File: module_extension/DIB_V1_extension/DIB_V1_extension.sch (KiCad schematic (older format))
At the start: 12 parts, among them J1 20-pin power socket, J3 28-pin module socket, J3 PROBE, J4 CABLE, J5 PROBE, J6 CABLE

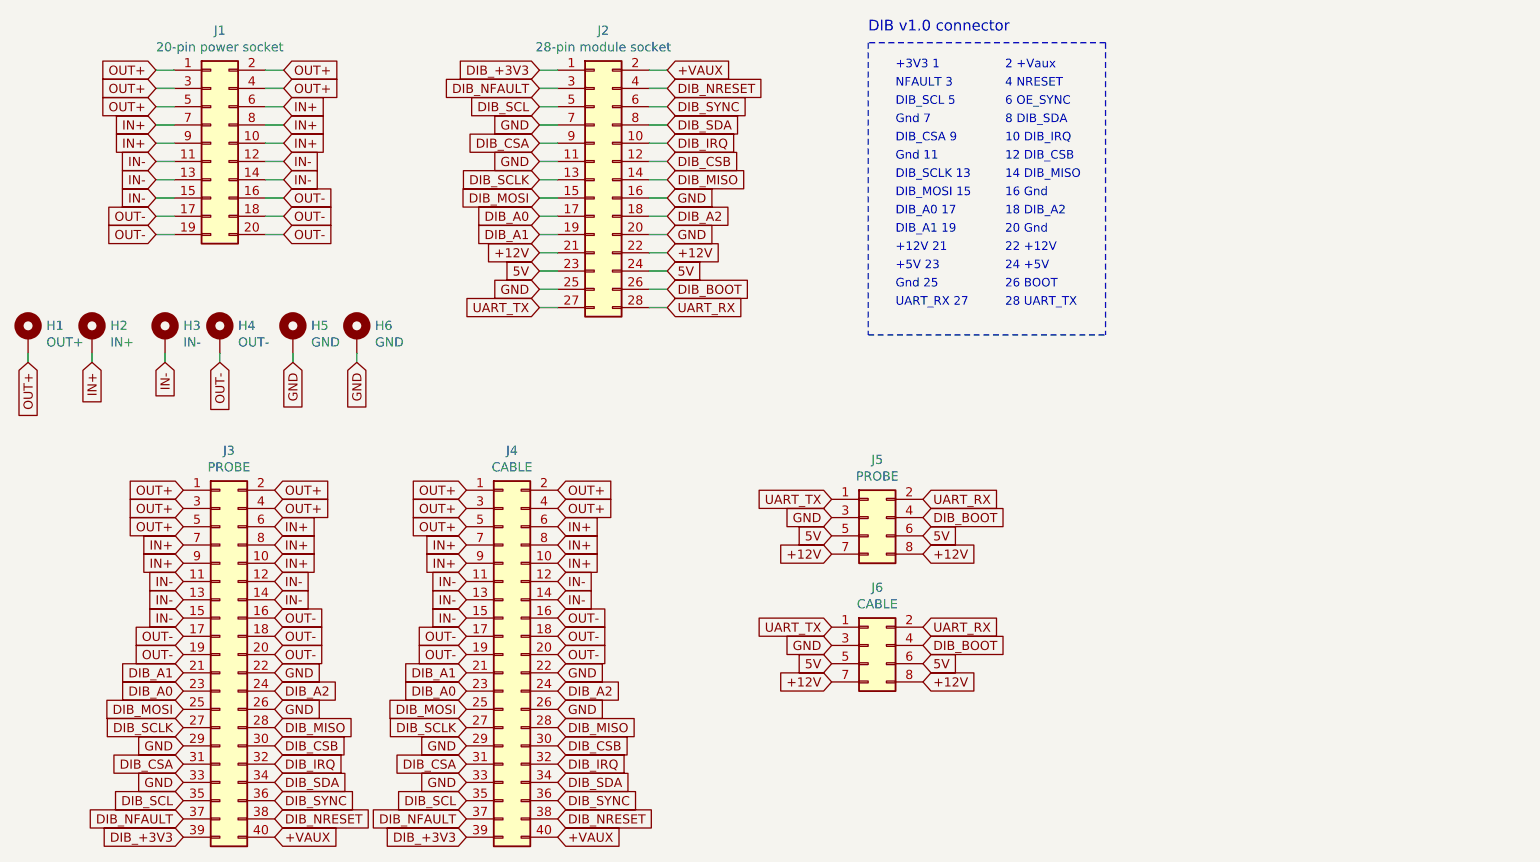
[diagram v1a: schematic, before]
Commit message: Changing pinout
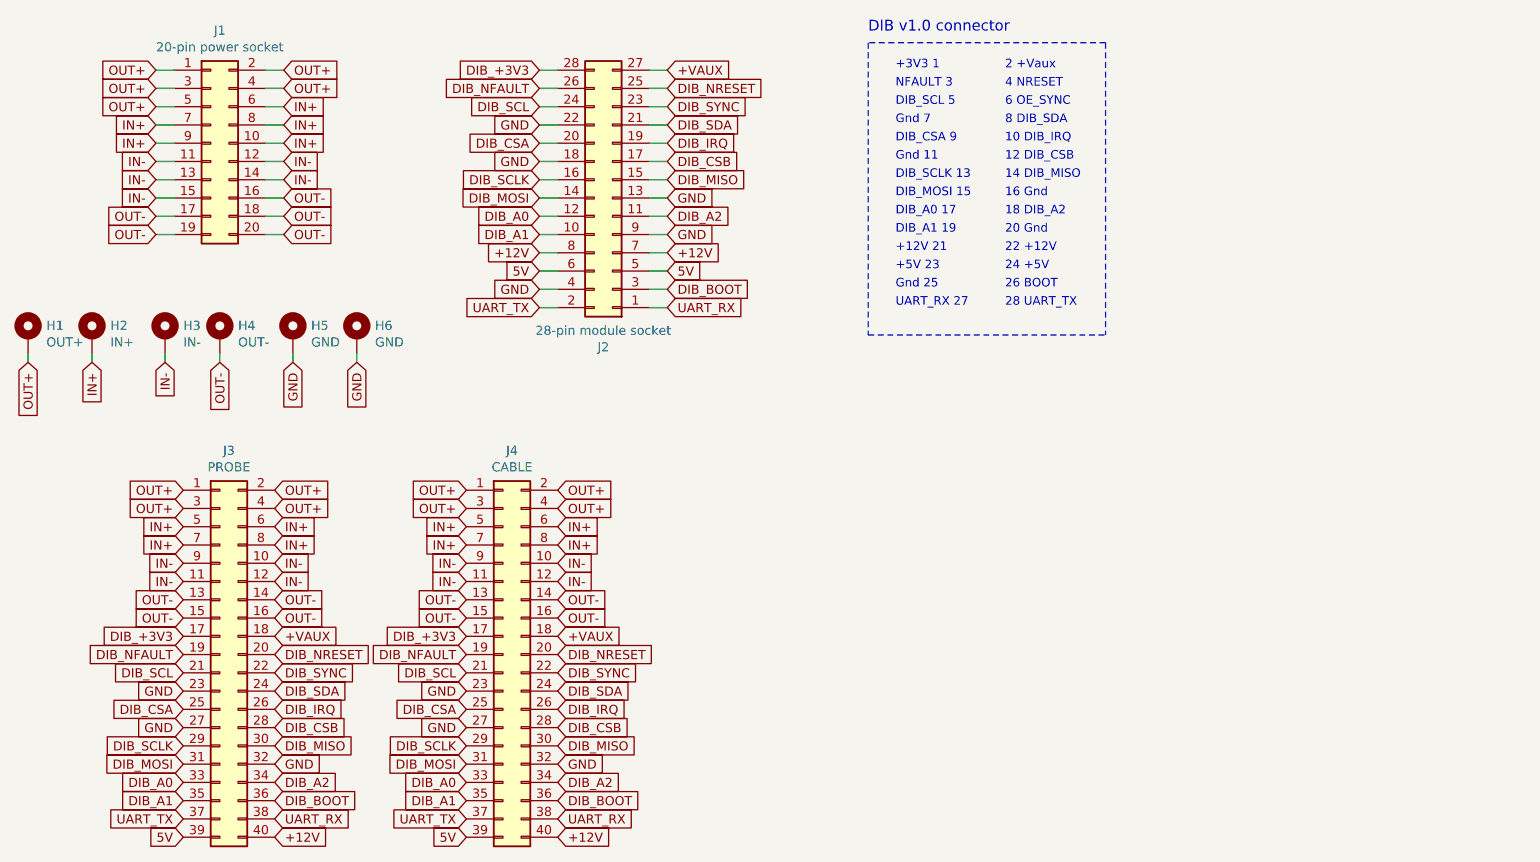
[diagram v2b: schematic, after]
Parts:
- removed J5: PROBE, Connector_PinHeader_2.54mm:PinHeader_2x04_P2.54mm_Vertical, symbol Connector_Generic:Conn_02x04_Odd_Even
- removed J6: CABLE, Connector_PinHeader_2.54mm:PinHeader_2x04_P2.54mm_Vertical, symbol Connector_Generic:Conn_02x04_Odd_Even
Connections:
- net +12V: now also J3.40 (Pin_40), J3.7 (Pin_7), J3.8 (Pin_8), J4.40 (Pin_40); no longer J3.21 (Pin_21), J3.22 (Pin_22)
- net +VAUX: now also J3.18 (Pin_18), J3.27 (Pin_27), J4.18 (Pin_18); no longer J3.2 (Pin_2), J3.40 (Pin_40), J4.40 (Pin_40)
- net 5V: now also J3.39 (Pin_39), J3.5 (Pin_5), J3.6 (Pin_6), J4.39 (Pin_39); no longer J3.23 (Pin_23), J3.24 (Pin_24)
- net DIB_+3V3: now also J3.17 (Pin_17), J3.28 (Pin_28), J4.17 (Pin_17); no longer J3.1 (Pin_1), J3.39 (Pin_39), J4.39 (Pin_39)
- net DIB_A0: now also J3.12 (Pin_12), J3.33 (Pin_33), J4.33 (Pin_33); no longer J3.17 (Pin_17), J3.23 (Pin_23), J4.23 (Pin_23)
- net DIB_A1: now also J3.10 (Pin_10), J3.35 (Pin_35), J4.35 (Pin_35); no longer J3.19 (Pin_19), J3.21 (Pin_21), J4.21 (Pin_21)
- net DIB_A2: now also J3.11 (Pin_11), J3.34 (Pin_34), J4.34 (Pin_34); no longer J3.18 (Pin_18), J3.24 (Pin_24), J4.24 (Pin_24)
- net DIB_BOOT: now also J3.3 (Pin_3), J3.36 (Pin_36), J4.36 (Pin_36); no longer J3.26 (Pin_26)
- net DIB_CSA: now also J3.20 (Pin_20), J3.25 (Pin_25), J4.25 (Pin_25); no longer J3.31 (Pin_31), J3.9 (Pin_9), J4.31 (Pin_31)
- net DIB_CSB: now also J3.17 (Pin_17), J3.28 (Pin_28), J4.28 (Pin_28); no longer J3.12 (Pin_12), J3.30 (Pin_30), J4.30 (Pin_30)
- net DIB_IRQ: now also J3.19 (Pin_19), J3.26 (Pin_26), J4.26 (Pin_26); no longer J3.10 (Pin_10), J3.32 (Pin_32), J4.32 (Pin_32)
- net DIB_MISO: now also J3.15 (Pin_15), J3.30 (Pin_30), J4.30 (Pin_30); no longer J3.14 (Pin_14), J3.28 (Pin_28), J4.28 (Pin_28)
- net DIB_MOSI: now also J3.14 (Pin_14), J3.31 (Pin_31), J4.31 (Pin_31); no longer J3.15 (Pin_15), J3.25 (Pin_25), J4.25 (Pin_25)
- net DIB_NFAULT: now also J3.19 (Pin_19), J3.26 (Pin_26), J4.19 (Pin_19); no longer J3.3 (Pin_3), J3.37 (Pin_37), J4.37 (Pin_37)
- net DIB_NRESET: now also J3.20 (Pin_20), J3.25 (Pin_25), J4.20 (Pin_20); no longer J3.38 (Pin_38), J3.4 (Pin_4), J4.38 (Pin_38)
- net DIB_SCL: now also J3.21 (Pin_21), J3.24 (Pin_24), J4.21 (Pin_21); no longer J3.35 (Pin_35), J3.5 (Pin_5), J4.35 (Pin_35)
- net DIB_SCLK: now also J3.16 (Pin_16), J3.29 (Pin_29), J4.29 (Pin_29); no longer J3.13 (Pin_13), J3.27 (Pin_27), J4.27 (Pin_27)
- net DIB_SDA: now also J3.21 (Pin_21), J3.24 (Pin_24), J4.24 (Pin_24); no longer J3.34 (Pin_34), J3.8 (Pin_8), J4.34 (Pin_34)
- net DIB_SYNC: now also J3.22 (Pin_22), J3.23 (Pin_23), J4.22 (Pin_22); no longer J3.36 (Pin_36), J3.6 (Pin_6), J4.36 (Pin_36)
- net GND: now also J3.13 (Pin_13), J3.18 (Pin_18), J3.22 (Pin_22), J3.23 (Pin_23), J3.27 (Pin_27), J3.32 (Pin_32), J3.4 (Pin_4), J3.9 (Pin_9), J4.23 (Pin_23), J4.27 (Pin_27), J4.32 (Pin_32); no longer J3.11 (Pin_11), J3.16 (Pin_16), J3.20 (Pin_20), J3.22 (Pin_22), J3.25 (Pin_25), J3.26 (Pin_26), J3.29 (Pin_29), J3.33 (Pin_33), J3.7 (Pin_7), J4.22 (Pin_22), J4.26 (Pin_26), J4.29 (Pin_29), J4.33 (Pin_33)
- net IN+: now also J3.5 (Pin_5), J4.5 (Pin_5); no longer J3.10 (Pin_10), J3.9 (Pin_9), J4.10 (Pin_10), J4.9 (Pin_9)
- net IN-: now also J3.10 (Pin_10), J3.9 (Pin_9), J4.10 (Pin_10), J4.9 (Pin_9); no longer J3.13 (Pin_13), J3.14 (Pin_14), J3.15 (Pin_15), J4.13 (Pin_13), J4.14 (Pin_14), J4.15 (Pin_15)
- net OUT+: no longer J3.5 (Pin_5), J4.5 (Pin_5)
- net OUT-: now also J3.13 (Pin_13), J3.14 (Pin_14), J3.15 (Pin_15), J4.13 (Pin_13), J4.14 (Pin_14), J4.15 (Pin_15); no longer J3.17 (Pin_17), J3.18 (Pin_18), J3.19 (Pin_19), J3.20 (Pin_20), J4.17 (Pin_17), J4.18 (Pin_18), J4.19 (Pin_19), J4.20 (Pin_20)
- net UART_RX: now also J3.1 (Pin_1), J3.38 (Pin_38), J4.38 (Pin_38); no longer J3.28 (Pin_28)
- net UART_TX: now also J3.2 (Pin_2), J3.37 (Pin_37), J4.37 (Pin_37); no longer J3.27 (Pin_27)
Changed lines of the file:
@@
 L Connector_Generic:Conn_02x14_Odd_Even J?
 U 1 1 5E5A4832
-P 3900 1650
+P 4000 1750
 AR Path="/5E22D00E/5E5A4832" Ref="J?"  Part="1"
 AR Path="/5E22C9F9/5E5A4832" Ref="J3"  Part="1"
 AR Path="/5E5A4832" Ref="J2"  Part="1"
-F 0 "J2" H 3950 2467 50  0000 C CNN
-F 1 "28-pin module socket" H 3950 2376 50  0000 C CNN
-F 2 "Connector_PinHeader_2.54mm:PinHeader_2x14_P2.54mm_Horizontal" H 3900 1650 50  0001 C CNN
-F 3 "~" H 3900 1650 50  0001 C CNN
-	1    3900 1650
-	1    0    0    -1
+F 0 "J2" H 4050 2567 50  0000 C CNN
+F 1 "28-pin module socket" H 4050 2476 50  0000 C CNN
+F 2 "Connector_PinHeader_2.54mm:PinHeader_2x14_P2.54mm_Horizontal" H 4000 1750 50  0001 C CNN
+F 3 "~" H 4000 1750 50  0001 C CNN
+	1    4000 1750
+	-1   0    0    1
 $EndComp
 Text GLabel 4300 1050 2    50   Input ~ 0
@@
 	2250 2600 2250 2650
 $Comp
-L Connector_Generic:Conn_02x04_Odd_Even J5
-U 1 1 5FA27915
-P 5400 3500
-F 0 "J5" H 5450 3817 50  0000 C CNN
-F 1 "PROBE" H 5450 3726 50  0000 C CNN
-F 2 "Connector_PinHeader_2.54mm:PinHeader_2x04_P2.54mm_Vertical" H 5400 3500 50  0001 C CNN
-F 3 "~" H 5400 3500 50  0001 C CNN
-	1    5400 3500
-	1    0    0    -1
-$EndComp
-$Comp
-L Connector_Generic:Conn_02x04_Odd_Even J6
-U 1 1 5FA28A68
-P 5400 4200
-F 0 "J6" H 5450 4517 50  0000 C CNN
-F 1 "CABLE" H 5450 4426 50  0000 C CNN
-F 2 "Connector_PinHeader_2.54mm:PinHeader_2x04_P2.54mm_Vertical" H 5400 4200 50  0001 C CNN
-F 3 "~" H 5400 4200 50  0001 C CNN
-	1    5400 4200
-	1    0    0    -1
-$EndComp
-$Comp
 L Mechanical:MountingHole_Pad H6
 U 1 1 5FA29C86
@@
 IN+
 Text GLabel 2150 3750 2    50   Input ~ 0
-IN+
+IN-
 Text GLabel 2150 3850 2    50   Input ~ 0
 IN-
 Text GLabel 2150 3950 2    50   Input ~ 0
-IN-
+OUT-
 Text GLabel 2150 4050 2    50   Input ~ 0
 OUT-
+Text GLabel 1650 3350 0    50   Input ~ 0
+OUT+
+Text GLabel 1650 3550 0    50   Input ~ 0
+IN+
+Text GLabel 1650 3450 0    50   Input ~ 0
+OUT+
+Text GLabel 1650 3650 0    50   Input ~ 0
+IN+
+Text GLabel 1650 3750 0    50   Input ~ 0
+IN-
+Text GLabel 1650 3850 0    50   Input ~ 0
+IN-
+Text GLabel 1650 3950 0    50   Input ~ 0
+OUT-
+Text GLabel 1650 4050 0    50   Input ~ 0
+OUT-
+Text GLabel 3200 3350 0    50   Input ~ 0
+OUT+
+Text GLabel 3200 3550 0    50   Input ~ 0
+IN+
+Text GLabel 3200 3450 0    50   Input ~ 0
+OUT+
+Text GLabel 3200 3650 0    50   Input ~ 0
+IN+
+Text GLabel 3200 3750 0    50   Input ~ 0
+IN-
+Text GLabel 3200 3850 0    50   Input ~ 0
+IN-
+Text GLabel 3200 3950 0    50   Input ~ 0
+OUT-
+Text GLabel 3200 4050 0    50   Input ~ 0
+OUT-
+Text GLabel 3700 3350 2    50   Input ~ 0
+OUT+
+Text GLabel 3700 3450 2    50   Input ~ 0
+OUT+
+Text GLabel 3700 3550 2    50   Input ~ 0
+IN+
+Text GLabel 3700 3650 2    50   Input ~ 0
+IN+
+Text GLabel 3700 3750 2    50   Input ~ 0
+IN-
+Text GLabel 3700 3850 2    50   Input ~ 0
+IN-
+Text GLabel 3700 3950 2    50   Input ~ 0
+OUT-
+Text GLabel 3700 4050 2    50   Input ~ 0
+OUT-
+Text GLabel 1650 4150 0    50   Input ~ 0
+DIB_+3V3
+Text GLabel 1650 4250 0    50   Input ~ 0
+DIB_NFAULT
+Text GLabel 1650 4350 0    50   Input ~ 0
+DIB_SCL
+Text GLabel 1650 4450 0    50   Input ~ 0
+GND
+Text GLabel 1650 4650 0    50   Input ~ 0
+GND
+Text GLabel 1650 4550 0    50   Input ~ 0
+DIB_CSA
+Text GLabel 1650 4750 0    50   Input ~ 0
+DIB_SCLK
+Text GLabel 1650 4850 0    50   Input ~ 0
+DIB_MOSI
+Text GLabel 1650 4950 0    50   Input ~ 0
+DIB_A0
+Text GLabel 1650 5050 0    50   Input ~ 0
+DIB_A1
 Text GLabel 2150 4150 2    50   Input ~ 0
-OUT-
++VAUX
+Text GLabel 2150 4350 2    50   Input ~ 0
+DIB_SYNC
+Text GLabel 2150 4450 2    50   Input ~ 0
+DIB_SDA
+Text GLabel 2150 4550 2    50   Input ~ 0
+DIB_IRQ
+Text GLabel 2150 4650 2    50   Input ~ 0
+DIB_CSB
+Text GLabel 2150 4750 2    50   Input ~ 0
+DIB_MISO
+Text GLabel 2150 4850 2    50   Input ~ 0
+GND
+Text GLabel 2150 4950 2    50   Input ~ 0
+DIB_A2
+Text GLabel 3700 4150 2    50   Input ~ 0
++VAUX
+Text GLabel 3700 4250 2    50   Input ~ 0
+DIB_NRESET
+Text GLabel 3700 4350 2    50   Input ~ 0
+DIB_SYNC
+Text GLabel 3700 4450 2    50   Input ~ 0
+DIB_SDA
+Text GLabel 3700 4550 2    50   Input ~ 0
+DIB_IRQ
+Text GLabel 3700 4650 2    50   Input ~ 0
+DIB_CSB
+Text GLabel 3700 4750 2    50   Input ~ 0
+DIB_MISO
+Text GLabel 3700 4850 2    50   Input ~ 0
+GND
+Text GLabel 3700 4950 2    50   Input ~ 0
+DIB_A2
+Text GLabel 2150 5050 2    50   Input ~ 0
+DIB_BOOT
+Text GLabel 2150 5150 2    50   Input ~ 0
+UART_RX
+Text GLabel 2150 5250 2    50   Input ~ 0
++12V
+Text GLabel 1650 5250 0    50   Input ~ 0
+5V
+Text GLabel 1650 5150 0    50   Input ~ 0
+UART_TX
+Text GLabel 3200 5050 0    50   Input ~ 0
+DIB_A1
+Text GLabel 3200 4950 0    50   Input ~ 0
+DIB_A0
+Text GLabel 3200 4850 0    50   Input ~ 0
+DIB_MOSI
+Text GLabel 3200 4750 0    50   Input ~ 0
+DIB_SCLK
+Text GLabel 3200 4550 0    50   Input ~ 0
+DIB_CSA
+Text GLabel 3200 4650 0    50   Input ~ 0
+GND
+Text GLabel 3200 4450 0    50   Input ~ 0
+GND
+Text GLabel 3200 4350 0    50   Input ~ 0
+DIB_SCL
+Text GLabel 3200 4250 0    50   Input ~ 0
+DIB_NFAULT
+Text GLabel 3200 4150 0    50   Input ~ 0
+DIB_+3V3
 Text GLabel 2150 4250 2    50   Input ~ 0
-OUT-
-Text GLabel 1650 3350 0    50   Input ~ 0
-OUT+
-Text GLabel 1650 3650 0    50   Input ~ 0
-IN+
-Text GLabel 1650 3450 0    50   Input ~ 0
-OUT+
-Text GLabel 1650 3750 0    50   Input ~ 0
-IN+
-Text GLabel 1650 3550 0    50   Input ~ 0
-OUT+
-Text GLabel 1650 3850 0    50   Input ~ 0
-IN-
-Text GLabel 1650 3950 0    50   Input ~ 0
-IN-
-Text GLabel 1650 4050 0    50   Input ~ 0
-IN-
-Text GLabel 1650 4150 0    50   Input ~ 0
-OUT-
-Text GLabel 1650 4250 0    50   Input ~ 0
-OUT-
-Text GLabel 3200 3350 0    50   Input ~ 0
-OUT+
-Text GLabel 3200 3650 0    50   Input ~ 0
-IN+
-Text GLabel 3200 3450 0    50   Input ~ 0
-OUT+
-Text GLabel 3200 3750 0    50   Input ~ 0
-IN+
-Text GLabel 3200 3550 0    50   Input ~ 0
-OUT+
-Text GLabel 3200 3850 0    50   Input ~ 0
-IN-
-Text GLabel 3200 3950 0    50   Input ~ 0
-IN-
-Text GLabel 3200 4050 0    50   Input ~ 0
-IN-
-Text GLabel 3200 4150 0    50   Input ~ 0
-OUT-
-Text GLabel 3200 4250 0    50   Input ~ 0
-OUT-
-Text GLabel 3700 3350 2    50   Input ~ 0
-OUT+
-Text GLabel 3700 3450 2    50   Input ~ 0
-OUT+
-Text GLabel 3700 3550 2    50   Input ~ 0
-IN+
-Text GLabel 3700 3650 2    50   Input ~ 0
-IN+
-Text GLabel 3700 3750 2    50   Input ~ 0
-IN+
-Text GLabel 3700 3850 2    50   Input ~ 0
-IN-
-Text GLabel 3700 3950 2    50   Input ~ 0
-IN-
-Text GLabel 3700 4050 2    50   Input ~ 0
-OUT-
-Text GLabel 3700 4150 2    50   Input ~ 0
-OUT-
-Text GLabel 3700 4250 2    50   Input ~ 0
-OUT-
-Text GLabel 1650 5250 0    50   Input ~ 0
-DIB_+3V3
-Text GLabel 1650 5150 0    50   Input ~ 0
-DIB_NFAULT
-Text GLabel 1650 5050 0    50   Input ~ 0
-DIB_SCL
-Text GLabel 1650 4950 0    50   Input ~ 0
-GND
-Text GLabel 1650 4750 0    50   Input ~ 0
-GND
-Text GLabel 1650 4850 0    50   Input ~ 0
-DIB_CSA
-Text GLabel 1650 4650 0    50   Input ~ 0
-DIB_SCLK
-Text GLabel 1650 4550 0    50   Input ~ 0
-DIB_MOSI
-Text GLabel 1650 4450 0    50   Input ~ 0
-DIB_A0
-Text GLabel 1650 4350 0    50   Input ~ 0
-DIB_A1
-Text GLabel 2150 5250 2    50   Input ~ 0
-+VAUX
-Text GLabel 2150 5050 2    50   Input ~ 0
-DIB_SYNC
-Text GLabel 2150 4950 2    50   Input ~ 0
-DIB_SDA
-Text GLabel 2150 4850 2    50   Input ~ 0
-DIB_IRQ
-Text GLabel 2150 4750 2    50   Input ~ 0
-DIB_CSB
-Text GLabel 2150 4650 2    50   Input ~ 0
-DIB_MISO
-Text GLabel 2150 4550 2    50   Input ~ 0
-GND
-Text GLabel 2150 4450 2    50   Input ~ 0
-DIB_A2
-Text GLabel 2150 4350 2    50   Input ~ 0
-GND
-Text GLabel 3700 5250 2    50   Input ~ 0
-+VAUX
-Text GLabel 3700 5150 2    50   Input ~ 0
 DIB_NRESET
 Text GLabel 3700 5050 2    50   Input ~ 0
-DIB_SYNC
-Text GLabel 3700 4950 2    50   Input ~ 0
-DIB_SDA
-Text GLabel 3700 4850 2    50   Input ~ 0
-DIB_IRQ
-Text GLabel 3700 4750 2    50   Input ~ 0
-DIB_CSB
-Text GLabel 3700 4650 2    50   Input ~ 0
-DIB_MISO
-Text GLabel 3700 4550 2    50   Input ~ 0
-GND
-Text GLabel 3700 4450 2    50   Input ~ 0
-DIB_A2
-Text GLabel 3700 4350 2    50   Input ~ 0
-GND
-Text GLabel 5700 3500 2    50   Input ~ 0
 DIB_BOOT
-Text GLabel 5700 3400 2    50   Input ~ 0
+Text GLabel 3200 5150 0    50   Input ~ 0
+UART_TX
+Text GLabel 3700 5150 2    50   Input ~ 0
 UART_RX
-Text GLabel 5700 3700 2    50   Input ~ 0
+Text GLabel 3200 5250 0    50   Input ~ 0
+5V
+Text GLabel 3700 5250 2    50   Input ~ 0
 +12V
-Text GLabel 5700 3600 2    50   Input ~ 0
-5V
-Text GLabel 5700 4200 2    50   Input ~ 0
-DIB_BOOT
-Text GLabel 5700 4100 2    50   Input ~ 0
-UART_RX
-Text GLabel 5700 4400 2    50   Input ~ 0
-+12V
-Text GLabel 5700 4300 2    50   Input ~ 0
-5V
-Text GLabel 5200 3700 0    50   Input ~ 0
-+12V
-Text GLabel 5200 3600 0    50   Input ~ 0
-5V
-Text GLabel 5200 3500 0    50   Input ~ 0
-GND
-Text GLabel 5200 3400 0    50   Input ~ 0
-UART_TX
-Text GLabel 5200 4400 0    50   Input ~ 0
-+12V
-Text GLabel 5200 4300 0    50   Input ~ 0
-5V
-Text GLabel 5200 4200 0    50   Input ~ 0
-GND
-Text GLabel 5200 4100 0    50   Input ~ 0
-UART_TX
-Text GLabel 3200 4350 0    50   Input ~ 0
-DIB_A1
-Text GLabel 3200 4450 0    50   Input ~ 0
-DIB_A0
-Text GLabel 3200 4550 0    50   Input ~ 0
-DIB_MOSI
-Text GLabel 3200 4650 0    50   Input ~ 0
-DIB_SCLK
-Text GLabel 3200 4850 0    50   Input ~ 0
-DIB_CSA
-Text GLabel 3200 4750 0    50   Input ~ 0
-GND
-Text GLabel 3200 4950 0    50   Input ~ 0
-GND
-Text GLabel 3200 5050 0    50   Input ~ 0
-DIB_SCL
-Text GLabel 3200 5150 0    50   Input ~ 0
-DIB_NFAULT
-Text GLabel 3200 5250 0    50   Input ~ 0
-DIB_+3V3
-Text GLabel 2150 5150 2    50   Input ~ 0
-DIB_NRESET
 $EndSCHEMATC
